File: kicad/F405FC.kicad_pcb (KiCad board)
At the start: 4 copper layers, 36 x 36 mm, 158 parts, among them J1 USB4105-GF-A, J2 ESC, J3 HD VTX, J4 GPS, J5 ELRS, P1 VBAT, P10 LED_DIN, P11 5V, P13 5V, P14 BUZ_N, P15 UART5_TX, P16 UART5_RX, P17 UART6_TX, P18 UART6_RX, P19 MOTOR5, P2 GND, P20 MOTOR6, P21 MOTOR7, P22 MOTOR8, P23 RSSI_IN, P24 GND, P25 5V, P3 10V, P4 GND, P5 CAM1_VID, P6 CAM2_VID, P7 VTX_VID, P8 5V, P9 GND, Q1 PMV40UN2, Q2 NX7002AK, SW1 BOOT, U1 LMR38020FSDDAR, U10 W25N01GV, U11 TS5A3159A, U12 SN74LV1T125, U13 USBLC6-2SC6, U2 LMR38020FSDDAR, U3 STM32F405RGT6, U4 LP38692MP-3.3, U5 LP5907MFX-3.3, U6 ICM-42688-P, U7 BMI270, U8 BMP390, U9 IIS2MDC, Y1 8MHz

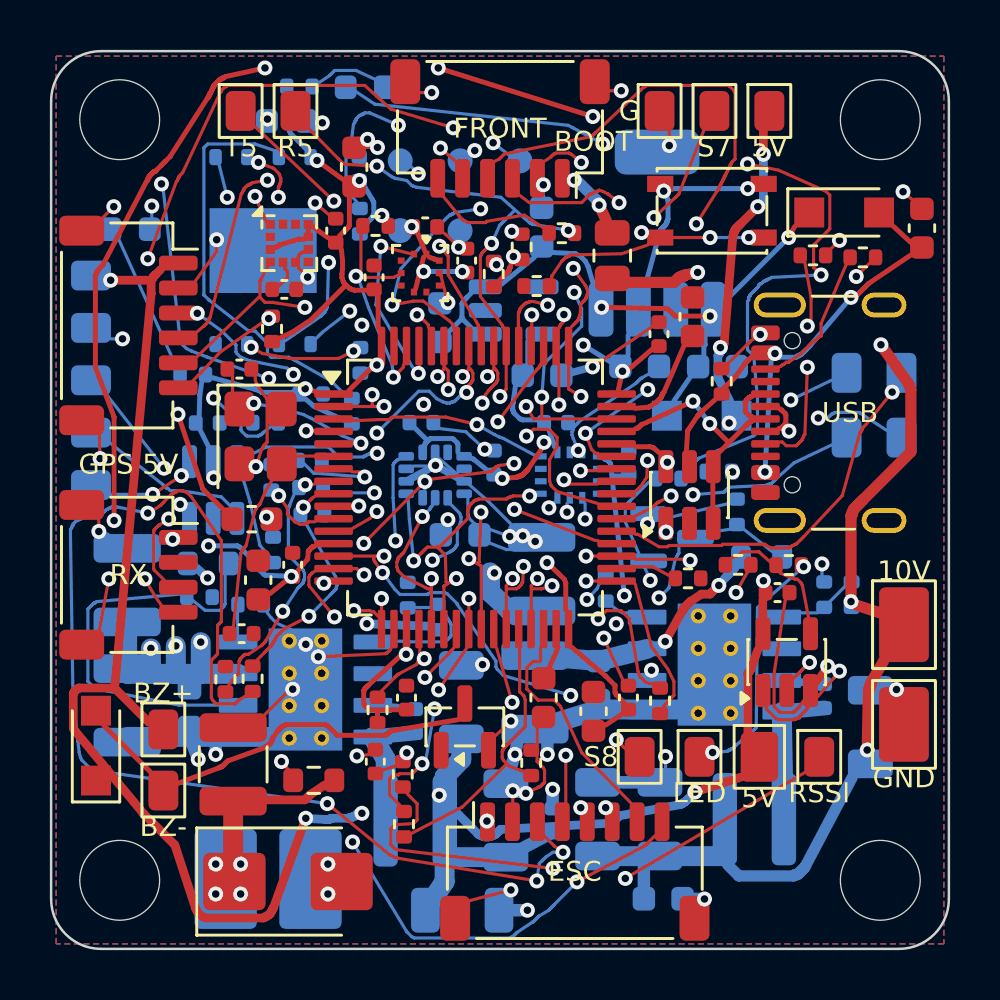
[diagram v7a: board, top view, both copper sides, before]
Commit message: Routing cleanup tooling: GND pass ties to tied copper, gndfan stub-vs-via check, prune step, tighter pours; docs updates
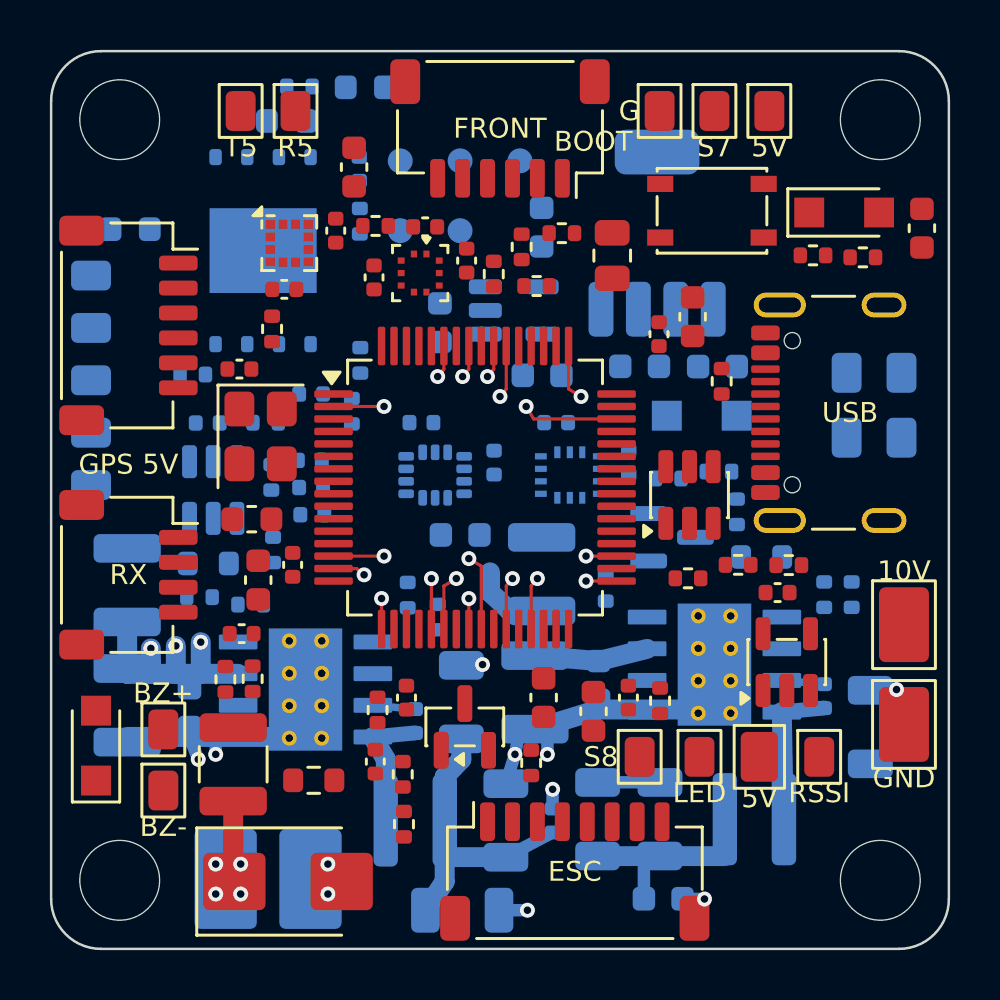
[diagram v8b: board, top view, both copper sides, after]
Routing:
- net GND: track 116.4 -> 24.6 mm, vias 60 -> 11
- net 5V: track 101.2 -> 10.5 mm, vias 11 -> 0
- net 3V3: track 81.6 -> 0.00 mm, vias 17 -> 0
- net 5V_SYS: track 63.1 -> 0.00 mm, vias 8 -> 0
- net VTX_PWR_EN: track 58.7 -> 0.00 mm, vias 3 -> 0
- net ESC_CURR: track 47.3 -> 0.00 mm, vias 4 -> 0
- net NRST: track 38.0 -> 0.00 mm, vias 4 -> 0
- net 10V: track 42.3 -> 6.81 mm, vias 4 -> 0
- net 3V3_IMU: track 33.4 -> 0.00 mm, vias 4 -> 0
- net STATUS_LED_BLUE: track 34.1 -> 1.22 mm, vias 3 -> 1
- net STATUS_LED_GREEN: track 31.5 -> 0.00 mm, vias 4 -> 0
- net ESC_TLM: track 29.3 -> 1.32 mm, vias 4 -> 1
- net UART1_RX: track 27.6 -> 0.00 mm, vias 3 -> 0
- net I2C1_SCL: track 23.8 -> 0.00 mm, vias 4 -> 0
- net RSSI_IN: track 21.0 -> 0.00 mm, vias 2 -> 0
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- removed copper zone on B.Cu, net GND
- removed copper zone on F.Cu, net GND
- removed copper zone on In2.Cu, net GND
